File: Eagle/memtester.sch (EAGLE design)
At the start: 4 parts

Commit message: Memtester: part work backup
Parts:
- added U$2, U$3: PCF8575TS, PCF8575TS:PCF8575TS
- U$1: value NN5118160AJ -> NN5118160AJSOCKET; device AtariST:NN5118160AJ -> memory:NN5118160AJSOCKET
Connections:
- new net A0: U$1.A0, U$3.P00
- new net A1: U$1.A1, U$3.P01
- new net A2: U$1.A2, U$3.P02
- new net A3: U$1.A3, U$3.P03
- new net A4: U$1.A4, U$3.P04
- new net A5: U$1.A5, U$3.P05
- new net A6: U$1.A6, U$3.P06
- new net A7: U$1.A7, U$3.P07
- new net A8: U$1.A8, U$3.P10
- new net A9: U$1.A9, U$3.P11
- new net D0: U$1.D0, U$2.P00
- new net D1: U$1.D1, U$2.P01
- new net D10: U$1.D10, U$2.P12
- new net D11: U$1.D11, U$2.P13
- new net D12: U$1.D12, U$2.P14
- new net D13: U$1.D13, U$2.P15
- new net D14: U$1.D14, U$2.P16
- new net D15: U$1.D15, U$2.P17
- new net D2: U$1.D2, U$2.P02
- new net D3: U$1.D3, U$2.P03
- new net D4: U$1.D4, U$2.P04
- new net D5: U$1.D5, U$2.P05
- new net D6: U$1.D6, U$2.P06
- new net D7: U$1.D7, U$2.P07
- new net D8: U$1.D8, U$2.P10
- new net D9: U$1.D9, U$2.P11
- new net I2C_SCL: U$2.SCL, U$3.SCL
- new net I2C_SDA: U$2.SDA, U$3.SDA
- net +5V: now also U$2.A0, U$2.A2, U$2.VCC, U$3.A2, U$3.VCC
- net GND: now also U$2.A1, U$2.GND, U$3.A0, U$3.A1, U$3.GND

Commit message: Memtester: part work
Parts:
- added C4: 100nF, resistor:C-EUC0402
- added C5, C6: 100nF, passives:CAPACITOR0402_CAP
- added IC1: HT7833, holtek2:HT7333
- added J3: SM08B-SRSS-TB(LF)(SN), SM08B-SRSS-TB_LF__SN_:SM08B-SRSS-TB(LF)(SN)
- added PROG: (no value), pinhead:PINHD-1X3
- added U$6: OLED_0.96_I2CNO_DRILL, tft_1_8_1_44_oled_0_96:OLED_0.96_I2CNO_DRILL
- added U1: ATTINY1616-MFR, ATTINY1616-MFR:ATTINY1616-MFR
- added UART: (no value), pinhead:PINHD-1X4
- C1, C2, C3: device rcl:C-EUC0805 -> passives:CAPACITOR0402_CAP
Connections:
- new net EXTCLK: U1.EXTCLK/PA3
- new net N$1: IC1.OUT, U$6.VCC
- new net OE: U$1./OE, U$3.P14
- new net PA5: U1.PA5
- new net PA6: U1.PA6
- new net PA7: U1.PA7
- new net PB2: U1.PB2/TOSC2
- new net PB3: U1.PB3/TOSC1
- new net PB4: U1.PB4
- new net PB5: U1.PB5
- new net RTS: U1.PA4
- new net RXD: U1.PA2, UART.2
- new net SPI_CS: J3.5, U1.PC3
- new net SPI_MISO: J3.6, U1.PC1
- new net SPI_MOSI: J3.3, U1.PC2
- new net SPI_SCLK: J3.4, U1.PC0
- new net TINY_RST: PROG.1, U1.PA0/!RESET!/UPDI
- new net TXD: U1.PA1, UART.1
- net +5V: now also C4.1, C5.1, C6.1, IC1.IN, J3.2, PROG.2, U1.VDD, UART.3
- net CAS0H: now also U$3.P13
- net CAS0L: now also U$3.P12
- net GND: now also C4.2, C5.2, C6.2, IC1.GND, J3.1, PROG.3, U$6.GND, U1.EXP, U1.GND, UART.4; no longer U$1./OE
- net I2C_SCL: now also J3.7, U$6.SCL, U1.PB0
- net I2C_SDA: now also J3.8, U$6.SDA, U1.PB1
- net WE: now also U$3.P15

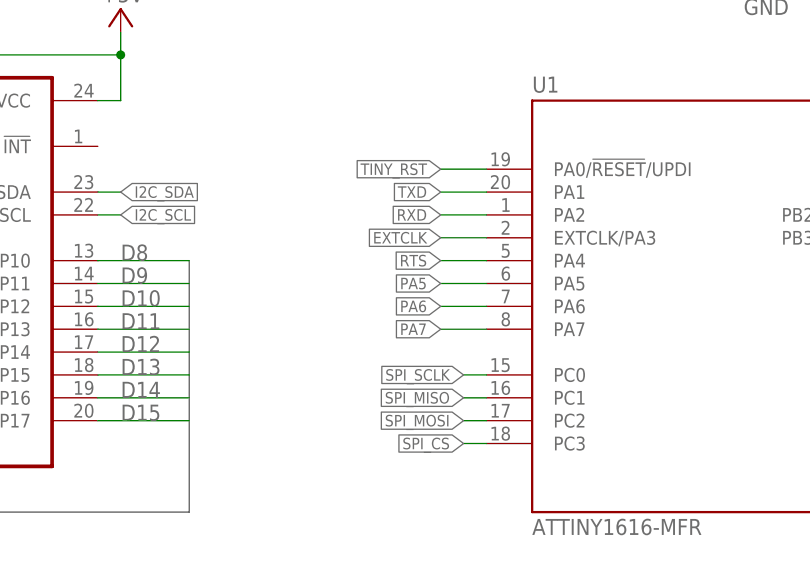
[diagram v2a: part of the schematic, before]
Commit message: Memtester: routed RAS0
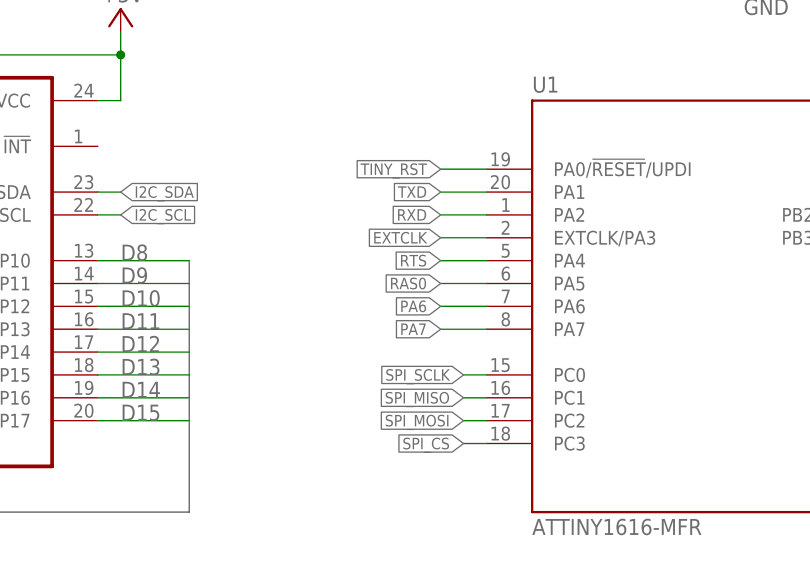
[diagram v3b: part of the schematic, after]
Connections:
- removed net PA5: U1.PA5
- net RAS0: now also U1.PA5
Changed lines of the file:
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@@
 <grid distance="0.1" unitdist="inch" unit="inch" style="lines" multiple="1" display="no" altdistance="0.01" altunitdist="inch" altunit="inch"/>
 <layers>
-<layer number="1" name="Top" color="4" fill="1" visible="yes" active="no"/>
-<layer number="2" name="Route2" color="16" fill="1" visible="yes" active="no"/>
-<layer number="15" name="Route15" color="23" fill="1" visible="yes" active="no"/>
-<layer number="16" name="Bottom" color="1" fill="1" visible="yes" active="no"/>
-<layer number="17" name="Pads" color="2" fill="1" visible="yes" active="no"/>
-<layer number="18" name="Vias" color="2" fill="1" visible="yes" active="no"/>
-<layer number="19" name="Unrouted" color="6" fill="1" visible="yes" active="no"/>
-<layer number="20" name="Dimension" color="24" fill="1" visible="yes" active="no"/>
-<layer number="21" name="tPlace" color="7" fill="1" visible="yes" active="no"/>
-<layer number="22" name="bPlace" color="7" fill="1" visible="yes" active="no"/>
-<layer number="23" name="tOrigins" color="15" fill="1" visible="yes" active="no"/>
-<layer number="24" name="bOrigins" color="15" fill="1" visible="yes" active="no"/>
-<layer number="25" name="tNames" color="7" fill="1" visible="yes" active="no"/>
-<layer number="26" name="bNames" color="7" fill="1" visible="yes" active="no"/>
-<layer number="27" name="tValues" color="7" fill="1" visible="yes" active="no"/>
-<layer number="28" name="bValues" color="7" fill="1" visible="yes" active="no"/>
+<layer number="1" name="Top" color="4" fill="1" visible="no" active="no"/>
+<layer number="2" name="Route2" color="16" fill="1" visible="no" active="no"/>
+<layer number="15" name="Route15" color="23" fill="1" visible="no" active="no"/>
+<layer number="16" name="Bottom" color="1" fill="1" visible="no" active="no"/>
+<layer number="17" name="Pads" color="2" fill="1" visible="no" active="no"/>
+<layer number="18" name="Vias" color="2" fill="1" visible="no" active="no"/>
+<layer number="19" name="Unrouted" color="6" fill="1" visible="no" active="no"/>
+<layer number="20" name="Dimension" color="24" fill="1" visible="no" active="no"/>
+<layer number="21" name="tPlace" color="7" fill="1" visible="no" active="no"/>
+<layer number="22" name="bPlace" color="7" fill="1" visible="no" active="no"/>
+<layer number="23" name="tOrigins" color="15" fill="1" visible="no" active="no"/>
+<layer number="24" name="bOrigins" color="15" fill="1" visible="no" active="no"/>
+<layer number="25" name="tNames" color="7" fill="1" visible="no" active="no"/>
+<layer number="26" name="bNames" color="7" fill="1" visible="no" active="no"/>
+<layer number="27" name="tValues" color="7" fill="1" visible="no" active="no"/>
+<layer number="28" name="bValues" color="7" fill="1" visible="no" active="no"/>
 <layer number="29" name="tStop" color="7" fill="3" visible="no" active="no"/>
 <layer number="30" name="bStop" color="7" fill="6" visible="no" active="no"/>
@@
 <layer number="35" name="tGlue" color="7" fill="4" visible="no" active="no"/>
 <layer number="36" name="bGlue" color="7" fill="5" visible="no" active="no"/>
-<layer number="37" name="tTest" color="7" fill="1" visible="yes" active="no"/>
-<layer number="38" name="bTest" color="7" fill="1" visible="yes" active="no"/>
+<layer number="37" name="tTest" color="7" fill="1" visible="no" active="no"/>
+<layer number="38" name="bTest" color="7" fill="1" visible="no" active="no"/>
 <layer number="39" name="tKeepout" color="4" fill="11" visible="no" active="no"/>
 <layer number="40" name="bKeepout" color="1" fill="11" visible="no" active="no"/>
@@
 <layer number="44" name="Drills" color="7" fill="1" visible="no" active="no"/>
 <layer number="45" name="Holes" color="7" fill="1" visible="no" active="no"/>
-<layer number="46" name="Milling" color="3" fill="1" visible="yes" active="no"/>
-<layer number="47" name="Measures" color="7" fill="1" visible="yes" active="no"/>
-<layer number="48" name="Document" color="7" fill="1" visible="yes" active="no"/>
-<layer number="49" name="Reference" color="7" fill="1" visible="yes" active="no"/>
-<layer number="50" name="dxf" color="7" fill="1" visible="yes" active="no"/>
-<layer number="51" name="tDocu" color="7" fill="1" visible="yes" active="no"/>
-<layer number="52" name="bDocu" color="7" fill="1" visible="yes" active="no"/>
-<layer number="53" name="tGND_GNDA" color="7" fill="1" visible="yes" active="no"/>
-<layer number="54" name="bGND_GNDA" color="7" fill="1" visible="yes" active="no"/>
-<layer number="56" name="wert" color="7" fill="1" visible="yes" active="no"/>
-<layer number="57" name="tCAD" color="7" fill="1" visible="yes" active="no"/>
+<layer number="46" name="Milling" color="3" fill="1" visible="no" active="no"/>
+<layer number="47" name="Measures" color="7" fill="1" visible="no" active="no"/>
+<layer number="48" name="Document" color="7" fill="1" visible="no" active="no"/>
+<layer number="49" name="Reference" color="7" fill="1" visible="no" active="no"/>
+<layer number="50" name="dxf" color="7" fill="1" visible="no" active="no"/>
+<layer number="51" name="tDocu" color="7" fill="1" visible="no" active="no"/>
+<layer number="52" name="bDocu" color="7" fill="1" visible="no" active="no"/>
+<layer number="53" name="tGND_GNDA" color="7" fill="1" visible="no" active="no"/>
+<layer number="54" name="bGND_GNDA" color="7" fill="1" visible="no" active="no"/>
+<layer number="56" name="wert" color="7" fill="1" visible="no" active="no"/>
+<layer number="57" name="tCAD" color="7" fill="1" visible="no" active="no"/>
 <layer number="58" name="bCAD" color="7" fill="1" visible="no" active="no"/>
-<layer number="59" name="tCarbon" color="7" fill="1" visible="yes" active="no"/>
-<layer number="60" name="bCarbon" color="7" fill="1" visible="yes" active="no"/>
+<layer number="59" name="tCarbon" color="7" fill="1" visible="no" active="no"/>
+<layer number="60" name="bCarbon" color="7" fill="1" visible="no" active="no"/>
 <layer number="88" name="SimResults" color="9" fill="1" visible="yes" active="yes"/>
 <layer number="89" name="SimProbes" color="9" fill="1" visible="yes" active="yes"/>
@@
 <pinref part="U$1" gate="G$1" pin="/RAS"/>
 </segment>
+<segment>
+<wire x1="109.22" y1="40.64" x2="104.14" y2="40.64" width="0.1524" layer="91"/>
+<label x="104.14" y="40.64" size="1.27" layer="95" rot="R180" xref="yes"/>
+<pinref part="U1" gate="G$1" pin="PA5"/>
+</segment>
 </net>
 <net name="CAS0H" class="0">
@@
 </segment>
 </net>
-<net name="PA5" class="0">
-<segment>
-<wire x1="109.22" y1="40.64" x2="104.14" y2="40.64" width="0.1524" layer="91"/>
-<label x="104.14" y="40.64" size="1.27" layer="95" rot="R180" xref="yes"/>
-<pinref part="U1" gate="G$1" pin="PA5"/>
-</segment>
-</net>

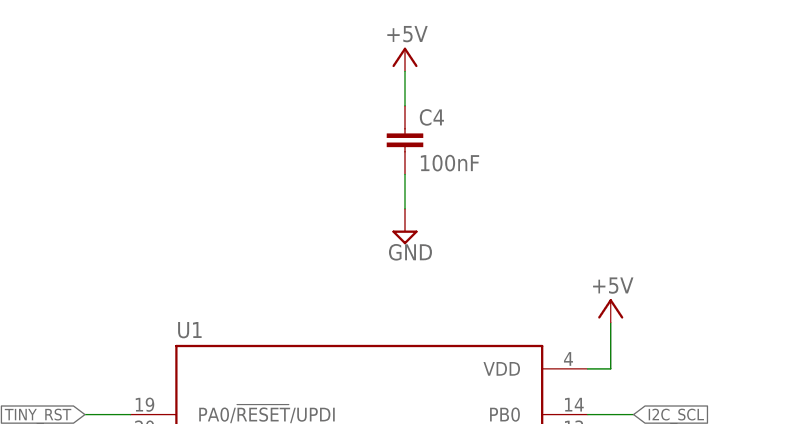
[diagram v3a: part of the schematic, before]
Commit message: Memtester: bigger 5v wire
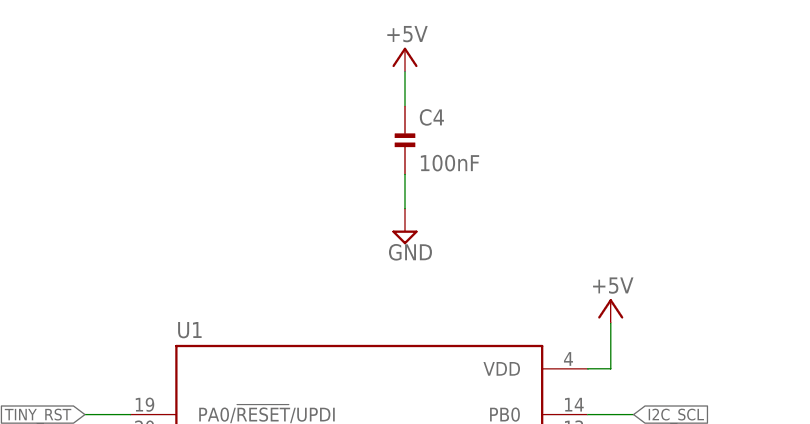
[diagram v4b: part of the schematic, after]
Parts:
- C4: device resistor:C-EUC0402 -> passives:CAPACITOR0402_CAP
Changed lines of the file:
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@@
 <drawing>
 <settings>
-<setting alwaysvectorfont="yes"/>
+<setting alwaysvectorfont="no"/>
 <setting verticaltext="up"/>
 </settings>
@@
 <part name="P+4" library="supply1" library_urn="urn:adsk.eagle:library:371" deviceset="+5V" device=""/>
 <part name="SUPPLY5" library="supply2" library_urn="urn:adsk.eagle:library:372" deviceset="GND" device=""/>
-<part name="C4" library="resistor" library_urn="urn:adsk.eagle:library:348" deviceset="C-EU" device="C0402" package3d_urn="urn:adsk.eagle:package:26136/1" value="100nF"/>
 <part name="P+5" library="supply1" library_urn="urn:adsk.eagle:library:371" deviceset="+5V" device=""/>
 <part name="SUPPLY6" library="supply2" library_urn="urn:adsk.eagle:library:372" deviceset="GND" device=""/>
@@
 <part name="SUPPLY13" library="supply2" library_urn="urn:adsk.eagle:library:372" deviceset="GND" device=""/>
 <part name="P+11" library="supply1" library_urn="urn:adsk.eagle:library:371" deviceset="+5V" device=""/>
+<part name="C4" library="passives" deviceset="CAPACITOR" device="0402_CAP" value="100nF"/>
 </parts>
 <sheets>
@@
 <attribute name="VALUE" x="160.655" y="6.985" size="1.778" layer="96"/>
 </instance>
-<instance part="C4" gate="G$1" x="139.7" y="85.09" smashed="yes">
-<attribute name="NAME" x="141.224" y="85.471" size="1.778" layer="95"/>
-<attribute name="VALUE" x="141.224" y="80.391" size="1.778" layer="96"/>
-</instance>
 <instance part="P+5" gate="1" x="139.7" y="93.98" smashed="yes">
 <attribute name="VALUE" x="142.24" y="96.52" size="1.778" layer="96" rot="R180"/>
@@
 <instance part="P+11" gate="1" x="114.3" y="-25.4" smashed="yes" rot="R90">
 <attribute name="VALUE" x="114.3" y="-22.86" size="1.778" layer="96" rot="R180"/>
+</instance>
+<instance part="C4" gate="G$1" x="139.7" y="85.09" smashed="yes">
+<attribute name="NAME" x="141.224" y="85.471" size="1.778" layer="95"/>
+<attribute name="VALUE" x="141.224" y="80.391" size="1.778" layer="96"/>
 </instance>
 </instances>
@@
 <segment>
 <pinref part="P+5" gate="1" pin="+5V"/>
+<wire x1="139.7" y1="91.44" x2="139.7" y2="87.63" width="0.1524" layer="91"/>
 <pinref part="C4" gate="G$1" pin="1"/>
-<wire x1="139.7" y1="91.44" x2="139.7" y2="87.63" width="0.1524" layer="91"/>
 </segment>
 <segment>
@@
 </segment>
 <segment>
-<pinref part="C4" gate="G$1" pin="2"/>
 <pinref part="SUPPLY6" gate="GND" pin="GND"/>
 <wire x1="139.7" y1="80.01" x2="139.7" y2="76.2" width="0.1524" layer="91"/>
-</segment>
-<segment>
+<pinref part="C4" gate="G$1" pin="2"/>
+</segment>
+<segment>
